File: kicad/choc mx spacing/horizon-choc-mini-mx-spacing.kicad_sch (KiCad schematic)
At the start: 102 parts, among them SW1 SW_Push, SW10 SW_Push, SW11 SW_Push, SW12 SW_Push, SW13 SW_Push, SW14 SW_Push, SW15 SW_Push, SW16 SW_Push, SW17 SW_Push, SW18 SW_Push, SW19 SW_Push, SW2 SW_Push, SW20 SW_Push, SW21 SW_Push, SW22 SW_Push, SW23 SW_Push, SW24 SW_Push, SW25 SW_Push, SW26 SW_Push, SW27 SW_Push, SW28 SW_Push, SW29 SW_Push, SW3 SW_Push, SW30 SW_Push, SW31 SW_Push, SW32 SW_Push, SW33 SW_Push, SW34 SW_Push, SW35 SW_Push, SW36 SW_Push, SW37 SW_Push, SW38 SW_Push, SW39 SW_Push, SW4 SW_Push, SW40 SW_Push, SW41 SW_Push, SW42 SW_Push, SW43 SW_Push, SW44 SW_Push, SW5 SW_Push, SW6 SW_Push, SW7 SW_Push, SW8 SW_Push, SW9 SW_Push, U3 Nice_Nano_V2

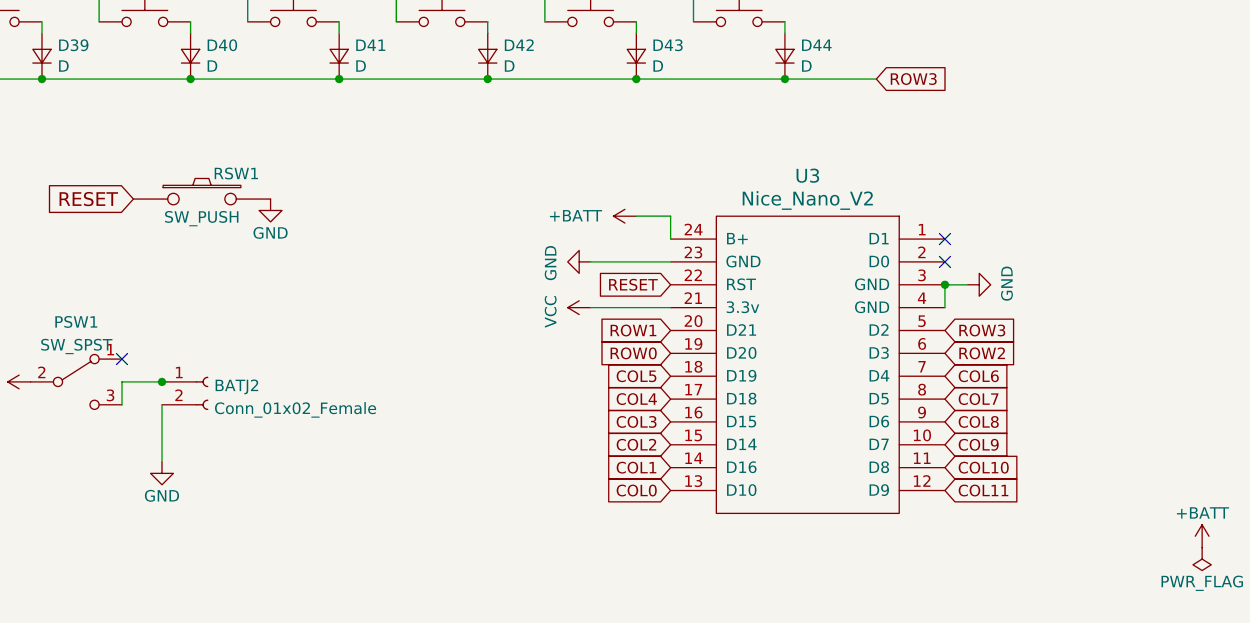
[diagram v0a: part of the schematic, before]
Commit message: - Updated and cleaned wiring - Added bottom plate holes for battery connector - New graphics (Tool heptagram) - Added teardrops - Added rubber feet markings - Made footprints more descriptive: diodes, switches - Sent to production!
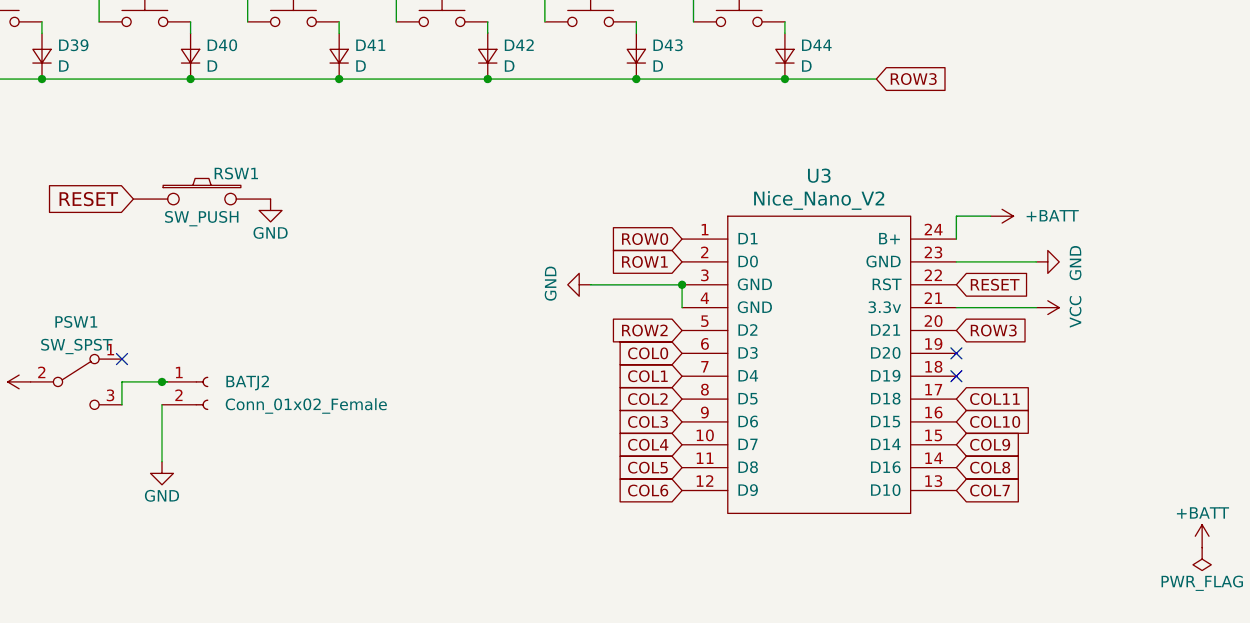
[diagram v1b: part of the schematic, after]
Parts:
- BATJ2: symbol Connector:Conn_01x02_Female -> Connector:Conn_01x02_Socket
- LOGO1: footprint horizon-footprints:Logo_Horizon_Small -> horizon-footprints:bloodborne_moon
- LOGO2: footprint horizon-footprints:Logo_Horizon_H -> horizon-footprints:bloodborne_moon
- SW1, SW10, SW11, SW12, SW13, SW14, SW15, SW16, SW17, SW18, SW19, SW2, SW20, SW21, SW22, SW23, SW24, SW25, SW26, SW27, SW28, SW29, SW3, SW30, SW31, SW32, SW33, SW34, SW35, SW36, SW37, SW38, SW39, SW4, SW40, SW41, SW42, SW43, SW44, SW5, SW6, SW7, SW8, SW9: footprint horizon-footprints:SW_Choc -> horizon-footprints:SW_Choc_MX
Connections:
- net COL0: now also U3.6 (D3); no longer U3.13 (D10)
- net COL1: now also U3.7 (D4); no longer U3.14 (D16)
- net COL10: now also U3.16 (D15); no longer U3.11 (D8)
- net COL11: now also U3.17 (D18); no longer U3.12 (D9)
- net COL2: now also U3.8 (D5); no longer U3.15 (D14)
- net COL3: now also U3.9 (D6); no longer U3.16 (D15)
- net COL4: now also U3.10 (D7); no longer U3.17 (D18)
- net COL5: now also U3.11 (D8); no longer U3.18 (D19)
- net COL6: now also U3.12 (D9); no longer U3.7 (D4)
- net COL7: now also U3.13 (D10); no longer U3.8 (D5)
- net COL8: now also U3.14 (D16); no longer U3.9 (D6)
- net COL9: now also U3.15 (D14); no longer U3.10 (D7)
- net ROW0: now also U3.1 (D1); no longer U3.19 (D20)
- net ROW1: now also U3.2 (D0); no longer U3.20 (D21)
- net ROW2: now also U3.5 (D2); no longer U3.6 (D3)
- net ROW3: now also U3.20 (D21); no longer U3.5 (D2)
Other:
- moved on the sheet: U3

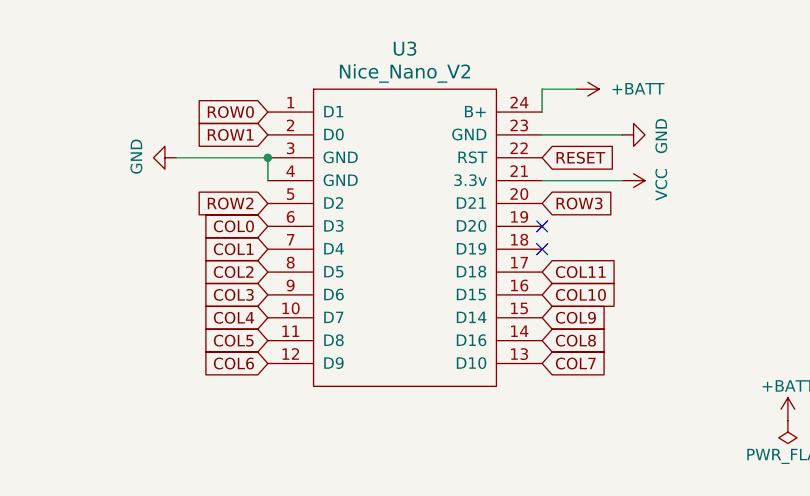
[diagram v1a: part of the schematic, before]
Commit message: - Fix flipped MCU footprint - Fix power switch label
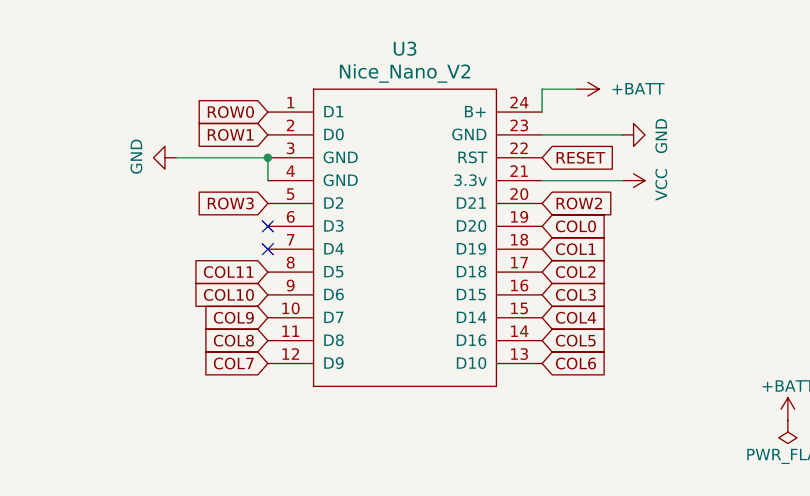
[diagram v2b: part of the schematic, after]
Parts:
- U3: footprint ScottoKeebs_MCU:Nice_Nano_V2 -> ScottoKeebs_MCU:Nice_Nano_V2_Flipped
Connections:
- net COL0: now also U3.19 (D20); no longer U3.6 (D3)
- net COL1: now also U3.18 (D19); no longer U3.7 (D4)
- net COL10: now also U3.9 (D6); no longer U3.16 (D15)
- net COL11: now also U3.8 (D5); no longer U3.17 (D18)
- net COL2: now also U3.17 (D18); no longer U3.8 (D5)
- net COL3: now also U3.16 (D15); no longer U3.9 (D6)
- net COL4: now also U3.15 (D14); no longer U3.10 (D7)
- net COL5: now also U3.14 (D16); no longer U3.11 (D8)
- net COL6: now also U3.13 (D10); no longer U3.12 (D9)
- net COL7: now also U3.12 (D9); no longer U3.13 (D10)
- net COL8: now also U3.11 (D8); no longer U3.14 (D16)
- net COL9: now also U3.10 (D7); no longer U3.15 (D14)
- net ROW2: now also U3.20 (D21); no longer U3.5 (D2)
- net ROW3: now also U3.5 (D2); no longer U3.20 (D21)
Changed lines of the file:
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@@
   (no_connect (at 85.09 138.43))
   (no_connect (at 138.43 137.795))
-  (no_connect (at 231.14 139.7))
-  (no_connect (at 231.14 137.16))
+  (no_connect (at 200.66 139.7))
+  (no_connect (at 200.66 137.16))
   (no_connect (at 85.09 129.54))
   (no_connect (at 57.15 138.43))
@@
     (stroke (width 0) (type default))
   )
-  (global_label "COL6" (shape input) (at 200.66 152.4 180) (fields_autoplaced)
-    (effects (font (size 1.27 1.27)) (justify right))
-    (property "Intersheetrefs" "${INTERSHEET_REFS}" (at 192.8367 152.4 0)
-      (effects (font (size 1.27 1.27)) (justify right) hide)
+  (global_label "COL3" (shape input) (at 231.14 144.78 0) (fields_autoplaced)
+    (effects (font (size 1.27 1.27)) (justify left))
+    (property "Intersheetrefs" "${INTERSHEET_REFS}" (at 238.9633 144.78 0)
+      (effects (font (size 1.27 1.27)) (justify left) hide)
     )
   )
-  (global_label "COL0" (shape input) (at 20.32 26.67 90) (fields_autoplaced)
+  (global_label "COL1" (shape input) (at 231.14 139.7 0) (fields_autoplaced)
     (effects (font (size 1.27 1.27)) (justify left))
-    (property "Intersheetrefs" "${INTERSHEET_REFS}" (at 20.32 19.5009 90)
+    (property "Intersheetrefs" "${INTERSHEET_REFS}" (at 238.9633 139.7 0)
       (effects (font (size 1.27 1.27)) (justify left) hide)
     )
   )
-  (global_label "COL1" (shape input) (at 200.66 139.7 180) (fields_autoplaced)
-    (effects (font (size 1.27 1.27)) (justify right))
-    (property "Intersheetrefs" "${INTERSHEET_REFS}" (at 192.8367 139.7 0)
-      (effects (font (size 1.27 1.27)) (justify right) hide)
+  (global_label "COL5" (shape input) (at 231.14 149.86 0) (fields_autoplaced)
+    (effects (font (size 1.27 1.27)) (justify left))
+    (property "Intersheetrefs" "${INTERSHEET_REFS}" (at 238.9633 149.86 0)
+      (effects (font (size 1.27 1.27)) (justify left) hide)
     )
   )
-  (global_label "COL3" (shape input) (at 200.66 144.78 180) (fields_autoplaced)
-    (effects (font (size 1.27 1.27)) (justify right))
-    (property "Intersheetrefs" "${INTERSHEET_REFS}" (at 192.8367 144.78 0)
-      (effects (font (size 1.27 1.27)) (justify right) hide)
+  (global_label "COL0" (shape input) (at 20.32 26.67 90) (fields_autoplaced)
+    (effects (font (size 1.27 1.27)) (justify left))
+    (property "Intersheetrefs" "${INTERSHEET_REFS}" (at 20.32 19.5009 90)
+      (effects (font (size 1.27 1.27)) (justify left) hide)
     )
   )
@@
     )
   )
-  (global_label "ROW0" (shape input) (at 222.25 45.72 0) (fields_autoplaced)
+  (global_label "COL2" (shape input) (at 231.14 142.24 0) (fields_autoplaced)
     (effects (font (size 1.27 1.27)) (justify left))
-    (property "Intersheetrefs" "${INTERSHEET_REFS}" (at 229.8424 45.72 0)
+    (property "Intersheetrefs" "${INTERSHEET_REFS}" (at 238.9633 142.24 0)
       (effects (font (size 1.27 1.27)) (justify left) hide)
     )
   )
-  (global_label "COL11" (shape input) (at 231.14 142.24 0) (fields_autoplaced)
+  (global_label "ROW0" (shape input) (at 222.25 45.72 0) (fields_autoplaced)
     (effects (font (size 1.27 1.27)) (justify left))
-    (property "Intersheetrefs" "${INTERSHEET_REFS}" (at 240.1728 142.24 0)
+    (property "Intersheetrefs" "${INTERSHEET_REFS}" (at 229.8424 45.72 0)
       (effects (font (size 1.27 1.27)) (justify left) hide)
     )
   )
-  (global_label "COL9" (shape input) (at 231.14 147.32 0) (fields_autoplaced)
-    (effects (font (size 1.27 1.27)) (justify left))
-    (property "Intersheetrefs" "${INTERSHEET_REFS}" (at 238.9633 147.32 0)
-      (effects (font (size 1.27 1.27)) (justify left) hide)
+  (global_label "COL11" (shape input) (at 200.66 142.24 180) (fields_autoplaced)
+    (effects (font (size 1.27 1.27)) (justify right))
+    (property "Intersheetrefs" "${INTERSHEET_REFS}" (at 191.6272 142.24 0)
+      (effects (font (size 1.27 1.27)) (justify right) hide)
     )
   )
@@
     )
   )
-  (global_label "COL0" (shape input) (at 200.66 137.16 180) (fields_autoplaced)
-    (effects (font (size 1.27 1.27)) (justify right))
-    (property "Intersheetrefs" "${INTERSHEET_REFS}" (at 192.8367 137.16 0)
-      (effects (font (size 1.27 1.27)) (justify right) hide)
-    )
-  )
   (global_label "COL2" (shape input) (at 53.34 26.67 90) (fields_autoplaced)
     (effects (font (size 1.27 1.27)) (justify left))
@@
     )
   )
-  (global_label "COL5" (shape input) (at 200.66 149.86 180) (fields_autoplaced)
+  (global_label "COL10" (shape input) (at 200.66 144.78 180) (fields_autoplaced)
     (effects (font (size 1.27 1.27)) (justify right))
-    (property "Intersheetrefs" "${INTERSHEET_REFS}" (at 192.8367 149.86 0)
+    (property "Intersheetrefs" "${INTERSHEET_REFS}" (at 191.6272 144.78 0)
       (effects (font (size 1.27 1.27)) (justify right) hide)
     )
   )
-  (global_label "ROW2" (shape input) (at 200.66 134.62 180) (fields_autoplaced)
+  (global_label "COL9" (shape input) (at 200.66 147.32 180) (fields_autoplaced)
     (effects (font (size 1.27 1.27)) (justify right))
-    (property "Intersheetrefs" "${INTERSHEET_REFS}" (at 193.0676 134.62 0)
+    (property "Intersheetrefs" "${INTERSHEET_REFS}" (at 192.8367 147.32 0)
       (effects (font (size 1.27 1.27)) (justify right) hide)
     )
   )
-  (global_label "COL7" (shape input) (at 231.14 152.4 0) (fields_autoplaced)
+  (global_label "COL0" (shape input) (at 231.14 137.16 0) (fields_autoplaced)
     (effects (font (size 1.27 1.27)) (justify left))
-    (property "Intersheetrefs" "${INTERSHEET_REFS}" (at 238.9633 152.4 0)
+    (property "Intersheetrefs" "${INTERSHEET_REFS}" (at 238.9633 137.16 0)
       (effects (font (size 1.27 1.27)) (justify left) hide)
     )
@@
     )
   )
+  (global_label "COL7" (shape input) (at 200.66 152.4 180) (fields_autoplaced)
+    (effects (font (size 1.27 1.27)) (justify right))
+    (property "Intersheetrefs" "${INTERSHEET_REFS}" (at 192.8367 152.4 0)
+      (effects (font (size 1.27 1.27)) (justify right) hide)
+    )
+  )
   (global_label "ROW0" (shape input) (at 200.66 124.46 180) (fields_autoplaced)
     (effects (font (size 1.27 1.27)) (justify right))
@@
     )
   )
-  (global_label "COL8" (shape input) (at 231.14 149.86 0) (fields_autoplaced)
-    (effects (font (size 1.27 1.27)) (justify left))
-    (property "Intersheetrefs" "${INTERSHEET_REFS}" (at 238.9633 149.86 0)
-      (effects (font (size 1.27 1.27)) (justify left) hide)
-    )
-  )
-  (global_label "COL10" (shape input) (at 231.14 144.78 0) (fields_autoplaced)
-    (effects (font (size 1.27 1.27)) (justify left))
-    (property "Intersheetrefs" "${INTERSHEET_REFS}" (at 240.1728 144.78 0)
-      (effects (font (size 1.27 1.27)) (justify left) hide)
-    )
-  )
   (global_label "ROW1" (shape input) (at 222.25 66.04 0) (fields_autoplaced)
     (effects (font (size 1.27 1.27)) (justify left))
@@
     )
   )
-  (global_label "ROW3" (shape input) (at 222.25 106.68 0) (fields_autoplaced)
-    (effects (font (size 1.27 1.27)) (justify left))
-    (property "Intersheetrefs" "${INTERSHEET_REFS}" (at 229.8424 106.68 0)
-      (effects (font (size 1.27 1.27)) (justify left) hide)
+  (global_label "COL8" (shape input) (at 200.66 149.86 180) (fields_autoplaced)
+    (effects (font (size 1.27 1.27)) (justify right))
+    (property "Intersheetrefs" "${INTERSHEET_REFS}" (at 192.8367 149.86 0)
+      (effects (font (size 1.27 1.27)) (justify right) hide)
     )
   )
-  (global_label "ROW3" (shape input) (at 231.14 134.62 0) (fields_autoplaced)
+  (global_label "ROW3" (shape input) (at 222.25 106.68 0) (fields_autoplaced)
     (effects (font (size 1.27 1.27)) (justify left))
-    (property "Intersheetrefs" "${INTERSHEET_REFS}" (at 239.3866 134.62 0)
+    (property "Intersheetrefs" "${INTERSHEET_REFS}" (at 229.8424 106.68 0)
       (effects (font (size 1.27 1.27)) (justify left) hide)
     )
   )
-  (global_label "COL4" (shape input) (at 200.66 147.32 180) (fields_autoplaced)
+  (global_label "ROW3" (shape input) (at 200.66 134.62 180) (fields_autoplaced)
     (effects (font (size 1.27 1.27)) (justify right))
-    (property "Intersheetrefs" "${INTERSHEET_REFS}" (at 192.8367 147.32 0)
+    (property "Intersheetrefs" "${INTERSHEET_REFS}" (at 192.4134 134.62 0)
       (effects (font (size 1.27 1.27)) (justify right) hide)
     )
@@
     )
   )
-  (global_label "COL2" (shape input) (at 200.66 142.24 180) (fields_autoplaced)
-    (effects (font (size 1.27 1.27)) (justify right))
-    (property "Intersheetrefs" "${INTERSHEET_REFS}" (at 192.8367 142.24 0)
-      (effects (font (size 1.27 1.27)) (justify right) hide)
+  (global_label "ROW2" (shape input) (at 231.14 134.62 0) (fields_autoplaced)
+    (effects (font (size 1.27 1.27)) (justify left))
+    (property "Intersheetrefs" "${INTERSHEET_REFS}" (at 239.3866 134.62 0)
+      (effects (font (size 1.27 1.27)) (justify left) hide)
     )
   )
@@
     )
   )
+  (global_label "COL6" (shape input) (at 231.14 152.4 0) (fields_autoplaced)
+    (effects (font (size 1.27 1.27)) (justify left))
+    (property "Intersheetrefs" "${INTERSHEET_REFS}" (at 238.9633 152.4 0)
+      (effects (font (size 1.27 1.27)) (justify left) hide)
+    )
+  )
   (global_label "COL11" (shape input) (at 201.93 26.67 90) (fields_autoplaced)
     (effects (font (size 1.27 1.27)) (justify left))
@@
     )
   )
+  (global_label "COL4" (shape input) (at 231.14 147.32 0) (fields_autoplaced)
+    (effects (font (size 1.27 1.27)) (justify left))
+    (property "Intersheetrefs" "${INTERSHEET_REFS}" (at 238.9633 147.32 0)
+      (effects (font (size 1.27 1.27)) (justify left) hide)
+    )
+  )
   (global_label "COL10" (shape input) (at 185.42 26.67 90) (fields_autoplaced)
     (effects (font (size 1.27 1.27)) (justify left))
@@
       (effects (font (size 1.524 1.524)))
     )
-    (property "Footprint" "ScottoKeebs_MCU:Nice_Nano_V2" (at 215.9 161.29 0)
+    (property "Footprint" "ScottoKeebs_MCU:Nice_Nano_V2_Flipped" (at 215.9 161.29 0)
       (effects (font (size 1.524 1.524)) hide)
     )
